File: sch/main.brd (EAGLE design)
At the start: 114.3 x 50.8 mm, 23 parts, among them IC2 PIC16F628P, T1 BC337, T2 BC337, T3 BC337, U1 YM1602G_LOWCON, X1 D-SUB9-H2M09ST

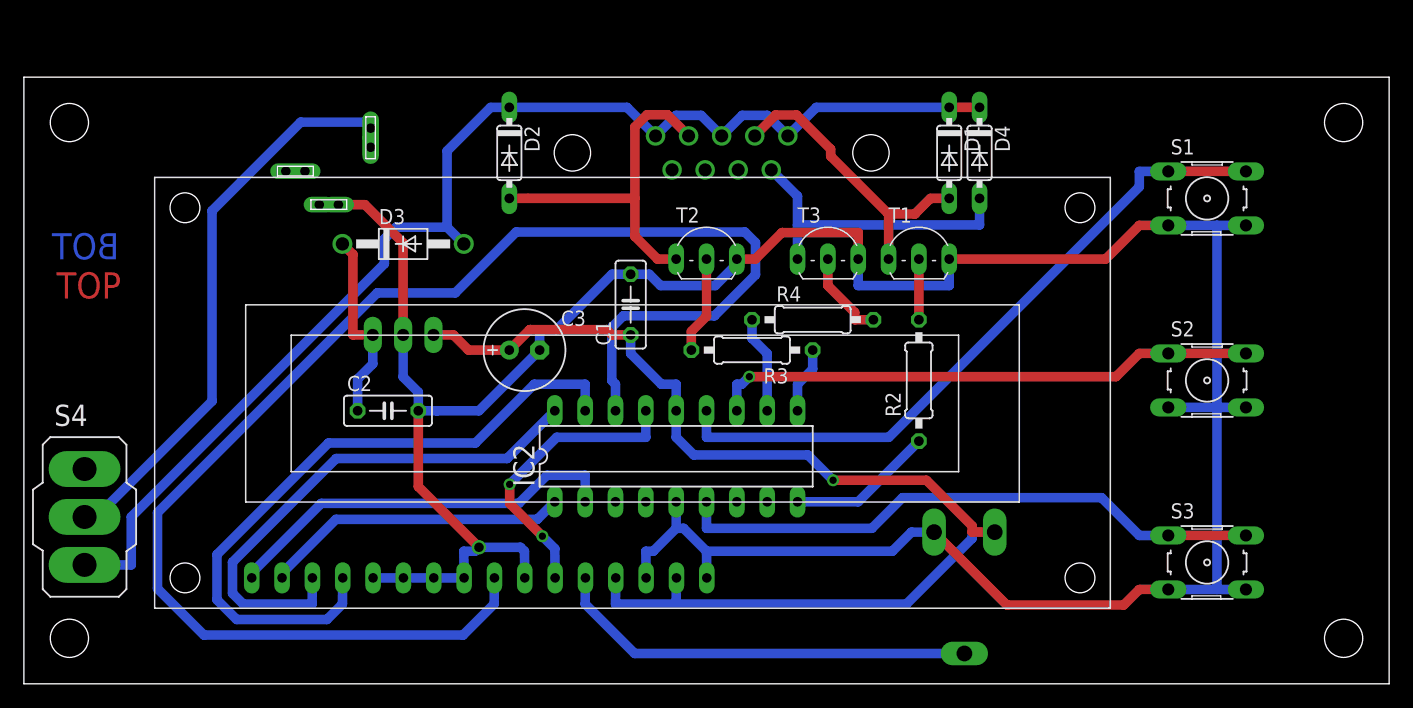
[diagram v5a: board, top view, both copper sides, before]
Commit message: Several packages change, re-routed
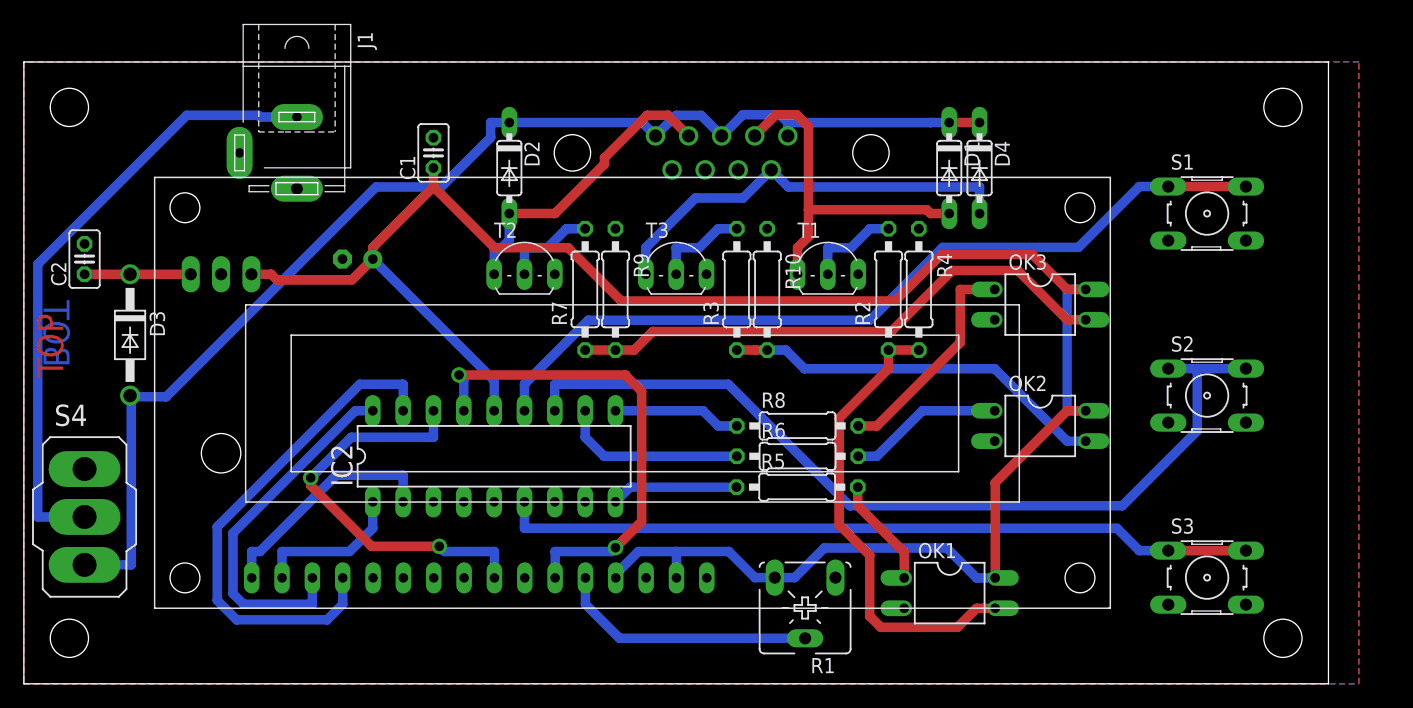
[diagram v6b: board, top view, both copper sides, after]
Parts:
- removed U$1: KLDVX-0202-A, con-kycon:KLDVX-0202-A
- added J1: (no value), con-jack:SPC4077
- added OK1, OK2, OK3: PC817, optocoupler:DIL04
- added R10, R9: 10k, rcl:0207/10
- added R5, R6, R8: 1k, rcl:0207/10
- added R7: 3k3, rcl:0207/10
- C1, C2: device rcl:C050-025X075 -> rcl:C025-025X050
- IC1: value (none) -> 7805; device v-reg:78XXS -> v-reg:78XXL
- R1: value (none) -> 4k7; device pot:CA9V -> pot:CA6V
- R2, R3: value 4k7 -> 3k3
- R4: value 4k7 -> 10k
- moved C2 28.4 mm to (3.81, 35.6), turned to 90 degrees
- moved D3 24.1 mm to (7.62, 29.2), turned to 270 degrees
- moved C1 20.8 mm to (33.0, 44.5)
- moved C3 15.9 mm to (26.7, 35.6), flipped to the bottom
- moved IC1 15.7 mm to (15.2, 30.5)
- moved T2 15.3 mm to (40.6, 34.3)
- moved IC2 15.2 mm to (38.1, 19.1)
- moved R1 13.4 mm to (64.1, 6.35), flipped to the top
- moved T3 12.8 mm to (53.3, 34.3)
- moved R4 9.25 mm to (73.7, 33.0), turned to 270 degrees
- moved R2 8.03 mm to (71.1, 33.0)
- moved T1 7.73 mm to (66.0, 34.3)
- moved R3 5.24 mm to (58.4, 33.0), turned to 90 degrees
- moved D1 1.27 mm to (76.2, 43.2)
- moved D2 1.27 mm to (39.4, 43.2)
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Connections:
- new net N$13: OK1.1, R5.2
- new net N$14: OK1.3, R2.1, R4.2
- new net N$15: OK2.3, R10.2, R3.1
- new net N$16: OK3.1, R8.2
- new net N$17: R7.2, T2.B
- new net N$18: OK3.3, R7.1, R9.2
- net +5V: now also OK1.4, OK2.4, OK3.4
- net GND: now also J1.3, OK1.2, OK2.2, OK3.2, R10.1, R4.1, R9.1; no longer U$1.2
- net N$10: now also R8.1; no longer R3.1
- net N$12: now also J1.1; no longer U$1.1
- net N$4: now also OK2.1, R6.2; no longer R3.2, T2.B
- net N$6: now also R5.1; no longer R2.1
- net N$7: now also R6.1; no longer R4.1
- net N$8: now also R3.2; no longer R4.2
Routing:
- net GND: track 236.8 -> 0.00 mm, vias 1 -> 0
- net E: track 123.2 -> 34.4 mm, vias 0 -> 2
- net +5V: track 98.0 -> 168.5 mm, vias 1 -> 0
- net N$18: track 0.00 -> 46.4 mm
- net N$14: track 0.00 -> 39.1 mm
- net N$15: track 0.00 -> 32.4 mm
- net SW2: track 45.9 -> 74.5 mm, vias 1 -> 0
- net N$16: track 0.00 -> 18.8 mm
- net RS: track 24.7 -> 40.4 mm
- net DB3: track 34.0 -> 19.7 mm
- net N$11: track 35.7 -> 21.8 mm
- net DB0: track 56.7 -> 42.8 mm
- net DB1: track 44.1 -> 30.2 mm
- net SW3: track 49.8 -> 63.4 mm
- net DB2: track 25.7 -> 12.8 mm
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- added copper zone on layer 1, net GND
- added copper zone on layer 16, net GND
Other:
- board size 114.3 x 50.8 mm -> 109.2 x 52.1 mm

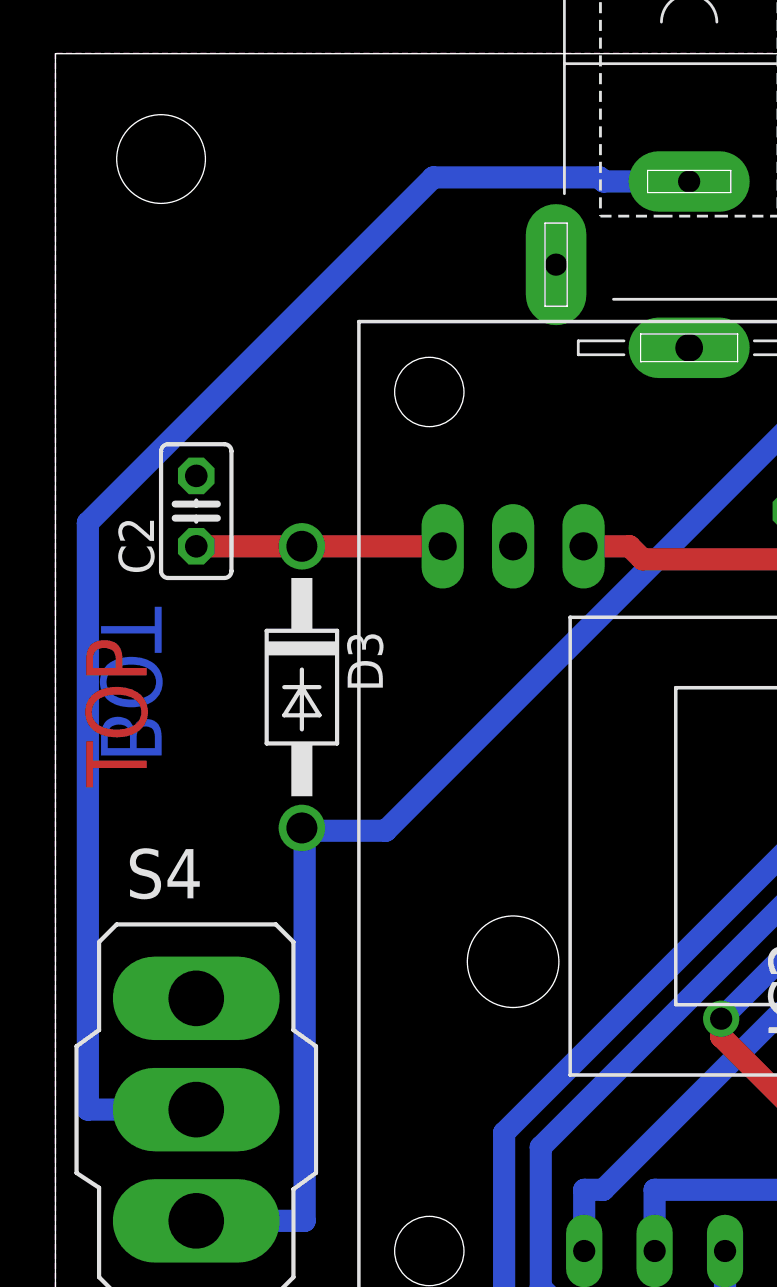
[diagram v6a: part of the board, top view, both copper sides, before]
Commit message: Added capacitor to power input
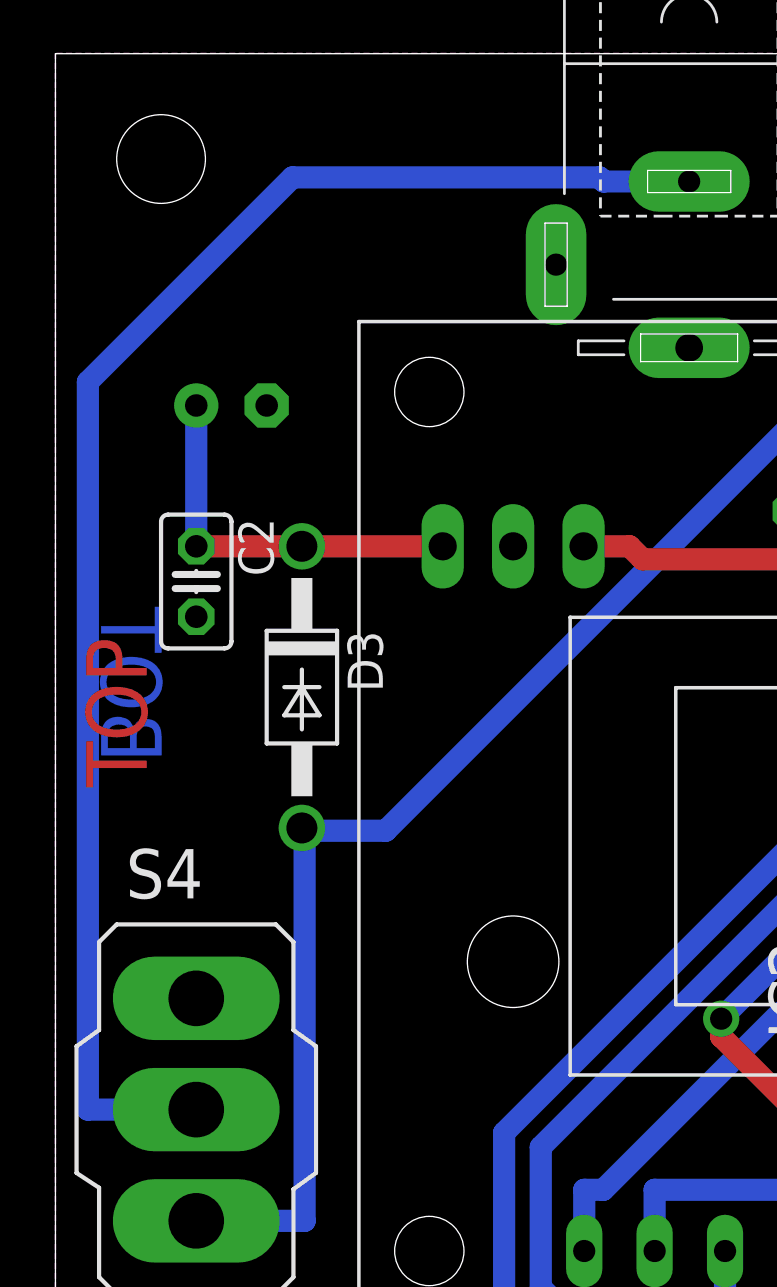
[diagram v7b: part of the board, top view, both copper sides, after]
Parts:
- added C4: 100u, rcl:E2,5-7
- moved C2 2.54 mm to (3.81, 33.0), turned to 270 degrees
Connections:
- net GND: now also C4.-
- net N$3: now also C4.+
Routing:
- net N$3: track 8.89 -> 14.0 mm
- net N$12: track 52.0 -> 55.0 mm
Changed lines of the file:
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@@
 <attribute name="OC_FARNELL" value="9760407" x="74.93" y="12.7" size="1.778" layer="27" display="off"/>
 </element>
-<element name="C2" library="rcl" package="C025-025X050" value="100n" x="3.81" y="35.56" rot="R90"/>
+<element name="C2" library="rcl" package="C025-025X050" value="100n" x="3.81" y="33.02" rot="R270"/>
 <element name="C3" library="rcl" package="E2,5-7" value="100u" x="26.67" y="35.56" rot="MR0"/>
 <element name="R2" library="rcl" package="0207/10" value="3k3" x="71.12" y="33.02" rot="R90"/>
@@
 <element name="R3" library="rcl" package="0207/10" value="3k3" x="58.42" y="33.02" rot="R90"/>
 <element name="R10" library="rcl" package="0207/10" value="10k" x="60.96" y="33.02" rot="R270"/>
+<element name="C4" library="rcl" package="E2,5-7" value="100u" x="5.08" y="39.37" rot="MR180"/>
 </elements>
 <signals>
@@
 <vertex x="110.49" y="52.07"/>
 </polygon>
+<contactref element="C4" pad="-"/>
 </signal>
 <signal name="+12V">
@@
 <wire x1="7.62" y1="34.29" x2="3.81" y2="34.29" width="0.8" layer="1"/>
 <wire x1="12.7" y1="34.29" x2="7.62" y2="34.29" width="0.8" layer="1"/>
+<contactref element="C4" pad="+"/>
+<wire x1="3.81" y1="34.29" x2="3.81" y2="39.37" width="0.8" layer="16"/>
 </signal>
 <signal name="N$6">
@@
 <wire x1="21.59" y1="47.45" x2="18.5055" y2="47.45" width="0.8" layer="16"/>
 <wire x1="3.81" y1="13.97" x2="-0.1001" y2="13.97" width="0.8" layer="16"/>
-<wire x1="-0.1001" y1="13.97" x2="-0.1001" y2="35.1381" width="0.8" layer="16"/>
-<wire x1="-0.1001" y1="35.1381" x2="12.3588" y2="47.597" width="0.8" layer="16"/>
-<wire x1="12.3588" y1="47.597" x2="18.3585" y2="47.597" width="0.8" layer="16"/>
+<wire x1="-0.1001" y1="13.97" x2="-0.1001" y2="40.2181" width="0.8" layer="16"/>
+<wire x1="-0.1001" y1="40.2181" x2="7.2788" y2="47.597" width="0.8" layer="16"/>
+<wire x1="7.2788" y1="47.597" x2="18.3585" y2="47.597" width="0.8" layer="16"/>
 <wire x1="18.3585" y1="47.597" x2="18.5055" y2="47.45" width="0.8" layer="16"/>
 </signal>
